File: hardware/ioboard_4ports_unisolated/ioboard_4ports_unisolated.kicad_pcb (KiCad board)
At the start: 2 copper layers, 106 x 55 mm, 56 parts, among them J1 Conn_02x06_Odd_Even, J10 XLR3, J11 XLR3, J12 Conn_01x03, J13 Conn_01x03, J14 8P8C, J2 XLR3, J3 XLR3, J4 XLR3, J5 XLR3, J6 Conn_01x03, J7 Conn_01x03, J8 XLR3, J9 XLR3, U1 M24C64-RMN6TP, U2 SP3485EN, U3 SP3485EN, U4 SP3485EN, U5 SP3485EN

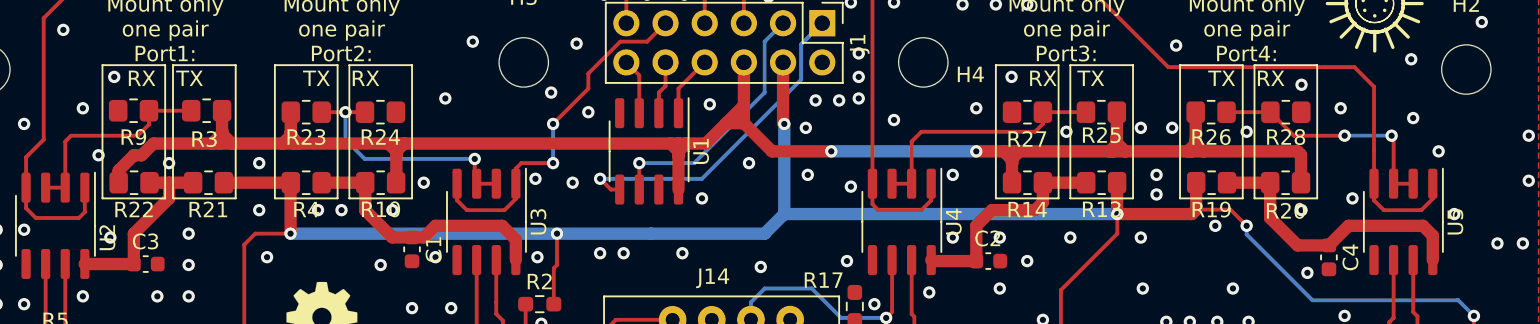
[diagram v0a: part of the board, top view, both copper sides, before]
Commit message: Update all footprints and ignore all other DRC warning on ioboards
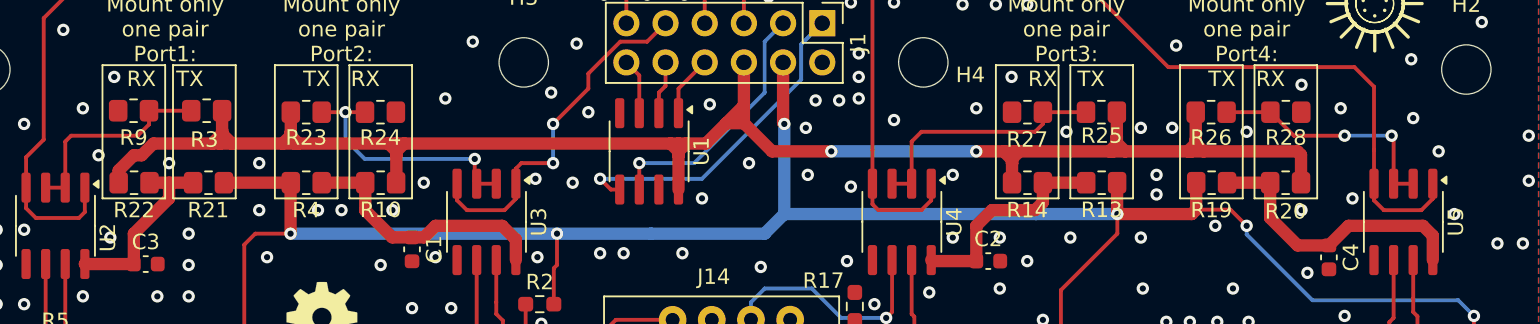
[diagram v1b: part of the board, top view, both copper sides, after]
